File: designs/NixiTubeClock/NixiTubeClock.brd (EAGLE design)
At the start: 53 x 92 mm, 15 parts, among them IC1 74141N, IC2 74HCT595D, IC3 74141N, IC4 74141N, IC5 74HCT595D, IC6 74141N

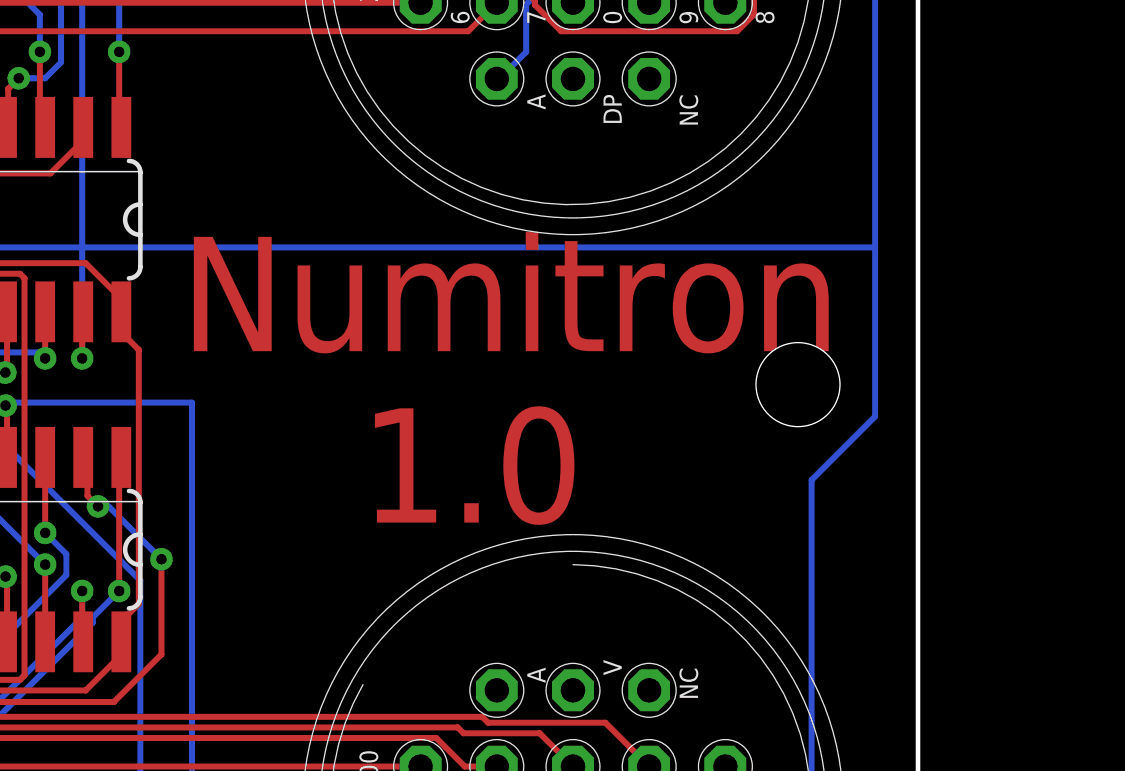
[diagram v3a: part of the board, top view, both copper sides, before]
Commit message: added parts for nixi clock final check during the week
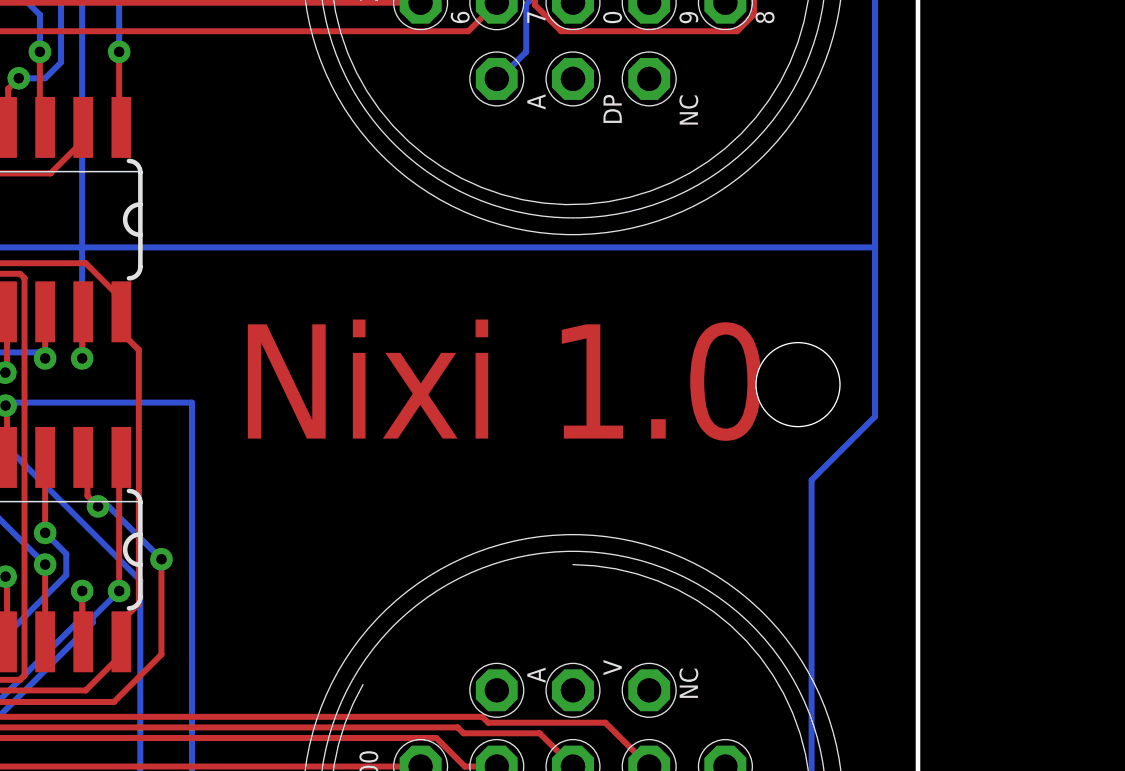
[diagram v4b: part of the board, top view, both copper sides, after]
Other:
- board text added: "Nixi 1.0"
- board text removed: "Numitron 1.0"
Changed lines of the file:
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@@
 </layers>
 <board>
-<fusionsync huburn="a.cGVyc29uYWw6dWUyYTNmMDU1" projecturn="a.cGVyc29uYWw6dWUyYTNmMDU1IzIwMTgxMjEwMTY0OTQ5MjI2" f3durn="urn:adsk.wipprod:dm.lineage:4VwSzylgQA2y2y0vYdfHkg" pcbguid="4cc8f609-dd40-4fe6-941d-2223811fa6e8" lastpulledtime="" lastsyncedchangeguid="e0bb74de-5975-9d3d-9985-4e0cd414534a"/>
+<fusionsync huburn="a.cGVyc29uYWw6dWUyYTNmMDU1" projecturn="a.cGVyc29uYWw6dWUyYTNmMDU1IzIwMTgxMjEwMTY0OTQ5MjI2" f3durn="urn:adsk.wipprod:dm.lineage:4VwSzylgQA2y2y0vYdfHkg" pcbguid="4cc8f609-dd40-4fe6-941d-2223811fa6e8" lastpulledtime="" lastsyncedchangeguid="c453b0fe-85f6-5747-9bb8-5b861afb4267"/>
 <plain>
 <wire x1="1" y1="89" x2="47" y2="89" width="0.1524" layer="20"/>
@@
 <text x="6.8" y="82.4" size="2.54" layer="29" font="vector" ratio="10">Moritz</text>
 <text x="6.8" y="82.4" size="2.54" layer="39" font="vector" ratio="10">Moritz</text>
-<text x="27.4" y="38.4" size="3.81" layer="1" font="vector" ratio="20">Numitron
-    1.0 </text>
-<text x="27.4" y="38.4" size="3.81" layer="29" font="vector" ratio="20">Numitron
-    1.0 </text>
-<text x="27.4" y="38.4" size="3.81" layer="39" font="vector" ratio="20">Numitron
-    1.0 </text>
+<text x="29.2" y="41.2" size="3.81" layer="1" font="vector" ratio="20">Nixi 1.0 </text>
+<text x="29.2" y="41.2" size="3.81" layer="29" font="vector" ratio="20">Nixi 1.0 </text>
+<text x="29.2" y="41.2" size="3.81" layer="39" font="vector" ratio="20">Nixi 1.0 </text>
 </plain>
 <attributes>
@@
 </drawing>
 <compatibility>
-<note version="6.3" minversion="6.2.2" severity="warning">
-Since Version 6.2.2 text objects can contain more than one line,
-which will not be processed correctly with this version.
-</note>
 <note version="8.2" severity="warning">
 Since Version 8.2, EAGLE supports online libraries. The ids

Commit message: added new nixi clock design top board
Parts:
- removed SV1: (no value), con-lstb:MA08-1
- added JP1: (no value), pinhead:2X04/90
- added JP3: (no value), pinhead:2X05/90
- added SV2: (no value), con-lstb:MA12-1
- moved AN1 9.60 mm to (48.0, 63.0)
- moved AN2 9.60 mm to (48.0, 83.0)
- moved AN3 9.60 mm to (48.0, 35.0)
- moved AN4 9.60 mm to (48.0, 15.0)
- moved IC1 9.60 mm to (20.5, 68.0)
- moved IC2 9.60 mm to (28.5, 54.5)
- moved IC3 9.60 mm to (20.5, 82.0)
- moved IC4 9.60 mm to (20.5, 30.0)
- moved IC5 9.60 mm to (28.5, 43.5)
- moved IC6 9.60 mm to (20.5, 16.0)
- moved R1 9.60 mm to (54.5, 75.0)
- moved R2 9.60 mm to (54.5, 71.0)
- moved R3 9.60 mm to (54.5, 27.0)
- moved R4 9.60 mm to (54.5, 23.0)
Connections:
- new net 12V: JP1.8, SV2.11
- new net DS1: IC2.14, JP3.1, SV2.4
- new net DS2: JP3.2, SV2.7
- new net SCL1: JP3.3, SV2.6
- new net SCL2: JP3.4, SV2.9
- new net SDA1: JP3.5, SV2.5
- new net SDA2: JP3.6, SV2.8
- net 170V: now also JP1.1; no longer SV1.6
- net 5V: now also JP3.7, JP3.8, SV2.12; no longer SV1.4
- net DS: now also SV2.1; no longer IC2.14, SV1.1
- net GND: now also JP1.2, JP1.3, JP1.4, JP1.5, JP1.6, JP1.7, JP3.10, JP3.9, SV2.10; no longer SV1.5, SV1.7, SV1.8
- net SH_CP: now also SV2.2; no longer SV1.2
- net ST_CP: now also SV2.3; no longer SV1.3
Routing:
- net GND: track 133.0 -> 164.9 mm, vias 7 -> 8
- net DS: track 28.0 -> 0.00 mm, vias 2 -> 0
- net DS1: track 0.00 -> 28.0 mm, vias 0 -> 2
- net SH_CP: track 37.6 -> 24.0 mm
- net ST_CP: track 30.2 -> 17.9 mm
- net 5V: track 150.9 -> 158.4 mm, vias 0 -> 2
- net 12V: track 0.00 -> 6.16 mm
- net 170V: track 106.7 -> 108.1 mm, vias 2 -> 4
- net N$114: track 56.0 -> 55.3 mm
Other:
- board size 53 x 92 mm -> 59.5 x 98 mm
- board text added: "12V"
- board text added: "DS1"
- board text added: "DS2"
- board text added: "SCL1"
- board text added: "SCL2"
- board text added: "SDA1"
- board text added: "SDA2"

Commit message: started work on mainboard
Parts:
- moved AN1 6.00 mm to (54.0, 63.0)
- moved AN2 6.00 mm to (54.0, 83.0)
- moved AN3 6.00 mm to (54.0, 35.0)
- moved AN4 6.00 mm to (54.0, 15.0)
- moved IC1 6.00 mm to (26.5, 68.0)
- moved IC2 6.00 mm to (34.5, 54.5)
- moved IC3 6.00 mm to (26.5, 82.0)
- moved IC4 6.00 mm to (26.5, 30.0)
- moved IC5 6.00 mm to (34.5, 43.5)
- moved IC6 6.00 mm to (26.5, 16.0)
- moved R1 6.00 mm to (60.5, 75.0)
- moved R2 6.00 mm to (60.5, 71.0)
- moved R3 6.00 mm to (60.5, 27.0)
- moved R4 6.00 mm to (60.5, 23.0)
- moved JP1 3.00 mm to (3.50, 27.0)
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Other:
- board size 59.5 x 98 mm -> 63 x 98 mm

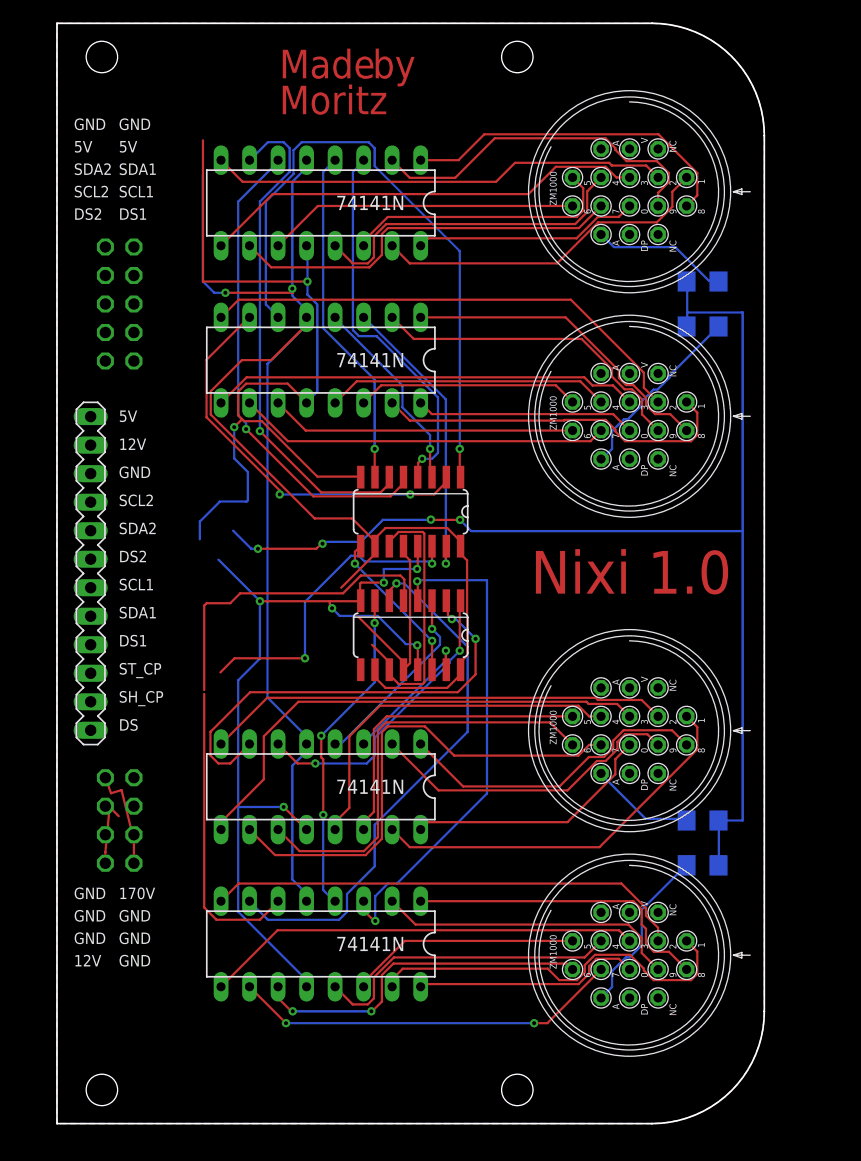
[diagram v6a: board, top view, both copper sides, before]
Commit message: added nixiClock brd and sheet with new design OSH
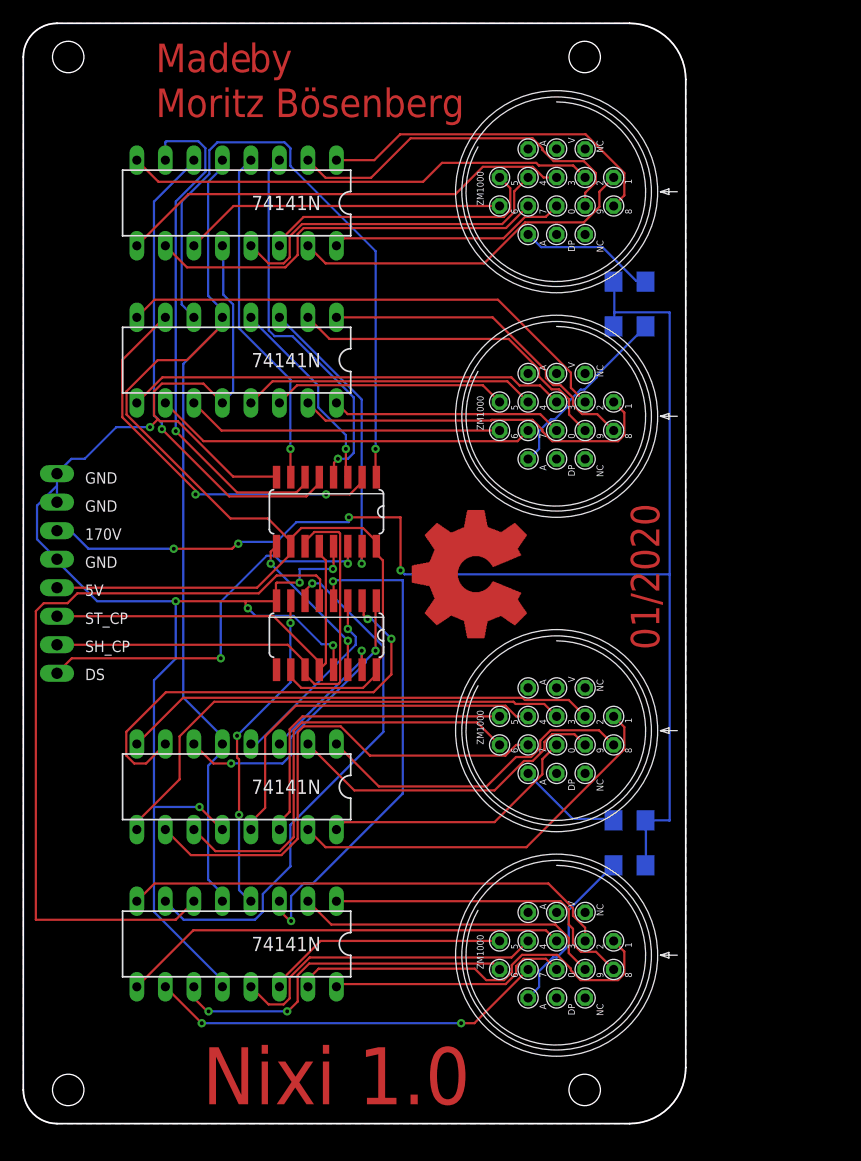
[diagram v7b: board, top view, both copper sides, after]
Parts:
- removed JP1: (no value), pinhead:2X04/90
- removed JP3: (no value), pinhead:2X05/90
- removed SV2: (no value), con-lstb:MA12-1
- added SV1: (no value), con-lstb:MA08-1
- moved IC1 7.50 mm to (19.0, 68.0)
- moved IC2 7.50 mm to (27.0, 54.5)
- moved IC3 7.50 mm to (19.0, 82.0)
- moved IC4 7.50 mm to (19.0, 30.0)
- moved IC5 7.50 mm to (27.0, 43.5)
- moved IC6 7.50 mm to (19.0, 16.0)
- moved AN1 6.50 mm to (47.5, 63.0)
- moved AN2 6.50 mm to (47.5, 83.0)
- moved AN3 6.50 mm to (47.5, 35.0)
- moved AN4 6.50 mm to (47.5, 15.0)
- moved R1 6.50 mm to (54.0, 75.0)
- moved R2 6.50 mm to (54.0, 71.0)
- moved R3 6.50 mm to (54.0, 27.0)
- moved R4 6.50 mm to (54.0, 23.0)
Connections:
- removed net 12V: JP1.8, SV2.11
- removed net DS1: IC2.14, JP3.1, SV2.4
- removed net DS2: JP3.2, SV2.7
- removed net SCL1: JP3.3, SV2.6
- removed net SCL2: JP3.4, SV2.9
- removed net SDA1: JP3.5, SV2.5
- removed net SDA2: JP3.6, SV2.8
- net 170V: now also SV1.6; no longer JP1.1
- net 5V: now also SV1.4; no longer JP3.7, JP3.8, SV2.12
- net DS: now also IC2.14, SV1.1; no longer SV2.1
- net GND: now also SV1.5, SV1.7, SV1.8; no longer JP1.2, JP1.3, JP1.4, JP1.5, JP1.6, JP1.7, JP3.10, JP3.9, SV2.10
- net SH_CP: now also SV1.2; no longer SV2.2
- net ST_CP: now also SV1.3; no longer SV2.3
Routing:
- net DS: track 0.00 -> 35.0 mm, vias 0 -> 2
- net DS1: track 28.0 -> 0.00 mm, vias 2 -> 0
- net SH_CP: track 24.0 -> 44.6 mm
- net ST_CP: track 17.9 -> 37.2 mm
- net GND: track 164.9 -> 146.8 mm, vias 8 -> 7
- net N$114: track 55.3 -> 71.0 mm
- net 170V: track 108.1 -> 122.0 mm
- net 12V: track 6.16 -> 0.00 mm
- net N$107: track 45.4 -> 46.4 mm
- net N$74: track 34.6 -> 35.6 mm
- net N$15: track 38.2 -> 39.2 mm
- net N$71: track 28.2 -> 29.2 mm
- net N$7: track 19.6 -> 20.6 mm
- net N$32: track 22.5 -> 23.5 mm
- net N$28: track 27.7 -> 28.7 mm
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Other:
- board size 63 x 98 mm -> 59 x 98 mm
- board text added: "01/2020"
- board text added: "Moritz Bösenberg"
- board text removed: "12V"
- board text removed: "DS1"
- board text removed: "DS2"
- board text removed: "Moritz"
- board text removed: "SCL1"
- board text removed: "SCL2"
- board text removed: "SDA1"
- board text removed: "SDA2"
